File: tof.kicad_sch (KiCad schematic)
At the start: 0 parts

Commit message: Initial component symbol placement
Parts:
- added U3: VL53L1CXV0FY/1, Library:OPTO-SMD_VL53L1CXV0FY-1, symbol Library:VL53L1CXV0FY_1
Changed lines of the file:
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@@
 	(generator_version "9.0")
 	(paper "A4")
+	(symbol
+		(lib_id "Library:VL53L1CXV0FY_1")
+		(at 143.51 99.06 90)
+		(unit 1)
+		(exclude_from_sim no)
+		(in_bom yes)
+		(on_board yes)
+		(dnp no)
+		(fields_autoplaced yes)
+		(property "Reference" "U3"
+			(at 145.6533 85.09 90)
+			(effects
+				(font
+					(size 1.27 1.27)
+				)
+				(justify right)
+			)
+		)
+		(property "Value" "VL53L1CXV0FY/1"
+			(at 145.6533 87.63 90)
+			(effects
+				(font
+					(size 1.27 1.27)
+				)
+				(justify right)
+			)
+		)
+		(property "Footprint" "Library:OPTO-SMD_VL53L1CXV0FY-1"
+			(at 171.45 99.06 0)
+			(effects
+				(font
+					(size 1.27 1.27)
+				)
+				(hide yes)
+			)
+		)
+		(property "Datasheet" "https://lcsc.com/product-detail/Sensors_STMicroelectronics_VL53L1CXV0FY-1_VL53L1CXV0FY-1_C190004.html"
+			(at 173.99 99.06 0)
+			(effects
+				(font
+					(size 1.27 1.27)
+				)
+				(hide yes)
+			)
+		)
+		(property "Description" ""
+			(at 143.51 99.06 0)
+			(effects
+				(font
+					(size 1.27 1.27)
+				)
+				(hide yes)
+			)
+		)
+		(property "Manufacturer" "ST(意法半导体)"
+			(at 176.53 99.06 0)
+			(effects
+				(font
+					(size 1.27 1.27)
+				)
+				(hide yes)
+			)
+		)
+		(property "MPN" "VL53L1CXV0FY/1"
+			(at 179.07 99.06 0)
+			(effects
+				(font
+					(size 1.27 1.27)
+				)
+				(hide yes)
+			)
+		)
+		(property "LCSC Part" "C190004"
+			(at 181.61 99.06 0)
+			(effects
+				(font
+					(size 1.27 1.27)
+				)
+				(hide yes)
+			)
+		)
+		(pin "5"
+		)
+		(pin "6"
+		)
+		(pin "7"
+		)
+		(pin "8"
+		)
+		(pin "2"
+		)
+		(pin "10"
+		)
+		(pin "11"
+		)
+		(pin "1"
+		)
+		(pin "12"
+		)
+		(pin "4"
+		)
+		(pin "9"
+		)
+		(pin "3"
+		)
+		(instances
+			(project ""
+				(path "/6af311bf-2fb1-446c-8c7e-7c930a463809/ea53fadf-30c4-4188-ad7c-32f8b223d643"
+					(reference "U3")
+					(unit 1)
+				)
+			)
+		)
+	)
 )

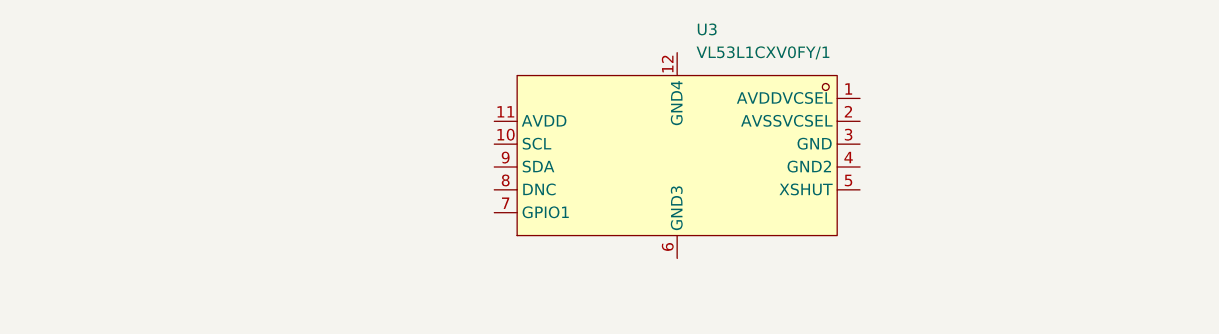
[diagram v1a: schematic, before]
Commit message: Barometer & ToF Hierarchical Schematic Updates
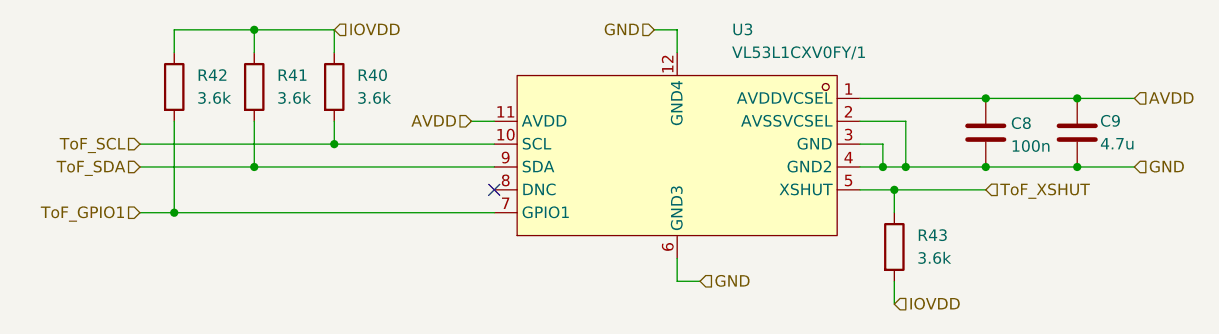
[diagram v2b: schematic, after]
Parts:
- added C8: 100n, symbol Device:C
- added C9: 4.7u, symbol Device:C
- added R40, R41, R42, R43: 3.6k, symbol Device:R
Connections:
- net AVDD: now reaches U3.1 (AVDDVCSEL)
- net AVDD: now also U3.11 (AVDD), C8.1, C9.1
- net ToF_SCL: now reaches U3.10 (SCL)
- net ToF_SCL: now also R40.2
- net GND: now reaches U3.12 (GND4)
- net GND: now also U3.2 (AVSSVCSEL), U3.3 (GND), U3.4 (GND2), U3.6 (GND3), C8.2, C9.2
- net ToF_XSHUT: now reaches U3.5 (XSHUT)
- net ToF_XSHUT: now also R43.1
- net ToF_GPIO1: now reaches U3.7 (GPIO1)
- net ToF_GPIO1: now also R42.2
- net ToF_SDA: now reaches U3.9 (SDA)
- net ToF_SDA: now also R41.2
- new net IOVDD: R40.1, R41.1, R42.1, R43.2
- no-connect marks 0 -> 1

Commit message: MCU implementation start Still needs component schematic checks & component integration with MCU
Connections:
- net AVDD renamed VDDA
- net IOVDD renamed +3.3V
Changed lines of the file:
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@@
 		)
 	)
-	(hierarchical_label "AVDD"
+	(hierarchical_label "VDDA"
 		(shape input)
 		(at 194.31 92.71 0)
@@
 		)
 	)
-	(hierarchical_label "IOVDD"
+	(hierarchical_label "+3.3V"
 		(shape input)
 		(at 105.41 85.09 0)
@@
 		)
 	)
-	(hierarchical_label "IOVDD"
+	(hierarchical_label "+3.3V"
 		(shape input)
 		(at 167.64 115.57 0)
@@
 		)
 	)
-	(hierarchical_label "AVDD"
+	(hierarchical_label "VDDA"
 		(shape input)
 		(at 120.65 95.25 180)

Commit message: MCU Integration & Sensor Ports
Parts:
- removed R40, R41, R42, R43: 3.6k, symbol Device:R
